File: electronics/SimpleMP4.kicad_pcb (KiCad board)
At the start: 2 copper layers, 136.9 x 66.4 mm, 130 parts, among them J1 USB_OTG, J2 DISPLAY, Q1 8050, Q2 SI2305, Q3 SI2305, Q4 8050, Q5 8550, Q6 SI2305, Q7 8550, U1 OCP8020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

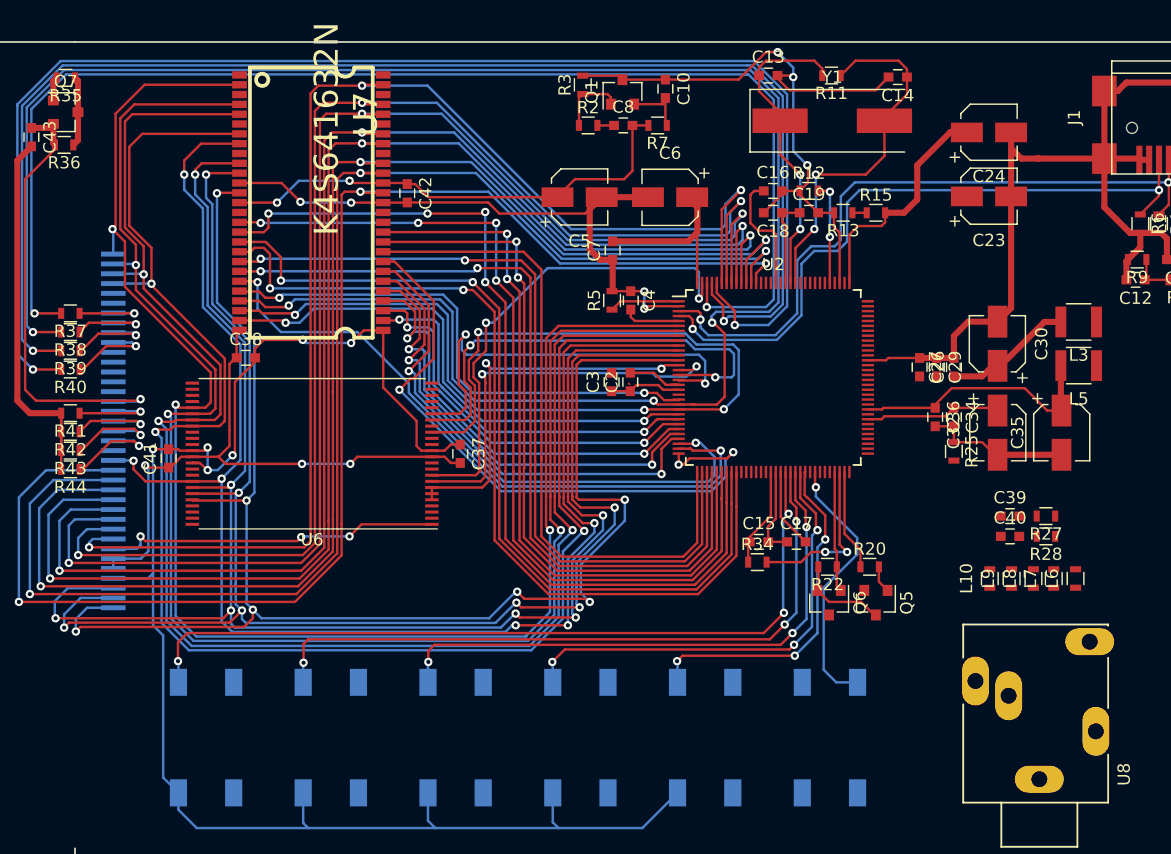
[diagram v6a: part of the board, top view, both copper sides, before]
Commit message: routed headphone jack
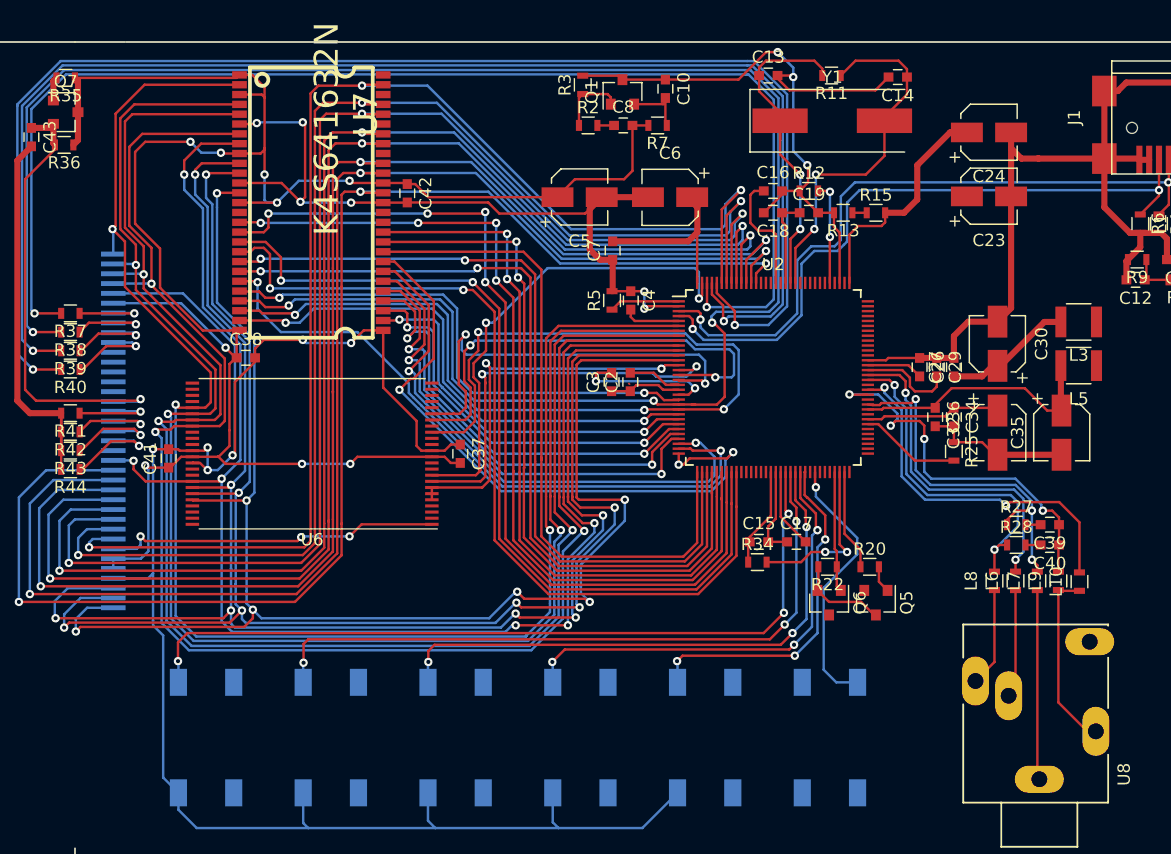
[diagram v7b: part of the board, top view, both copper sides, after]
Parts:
- moved L10 7.31 mm to (150.7, 170.3)
- moved L6 4.89 mm to (145.5, 170.2)
- moved L9 3.81 mm to (149.0, 170.2)
- moved C39 3.31 mm to (148.3, 165.7), turned to 180 degrees
- moved C40 3.31 mm to (148.3, 167.3), turned to 180 degrees
- moved L8 3.18 mm to (143.8, 170.2)
- moved R27 2.51 mm to (145.6, 165.7), turned to 0 degrees
- moved R28 2.51 mm to (145.6, 167.3), turned to 0 degrees
- moved L7 1.35 mm to (147.3, 170.2)
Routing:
- net VCC: track 174.1 -> 257.4 mm, vias 5 -> 11
- net GND: track 486.2 -> 518.8 mm, vias 18 -> 20
- net /AOM: track 0.00 -> 31.2 mm, vias 0 -> 4
- net /AOMS: track 0.00 -> 29.6 mm, vias 0 -> 2
- net /AOL: track 0.00 -> 29.0 mm, vias 0 -> 3
- net /AOR: track 0.00 -> 27.7 mm, vias 0 -> 2
- net /HP_SENSE: track 0.00 -> 27.1 mm, vias 0 -> 2
- net Net-(L7-Pad1): track 0.00 -> 15.5 mm
- net Net-(L10-Pad1): track 0.00 -> 14.9 mm
- net Net-(L6-Pad1): track 0.00 -> 8.84 mm
- net Net-(R25-Pad2): track 0.00 -> 8.24 mm
- net Net-(L8-Pad1): track 0.00 -> 8.05 mm
- net Net-(C29-Pad2): track 0.00 -> 7.73 mm
- net Net-(C26-Pad2): track 0.00 -> 4.59 mm
- net Net-(C40-Pad2): track 0.00 -> 1.23 mm
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
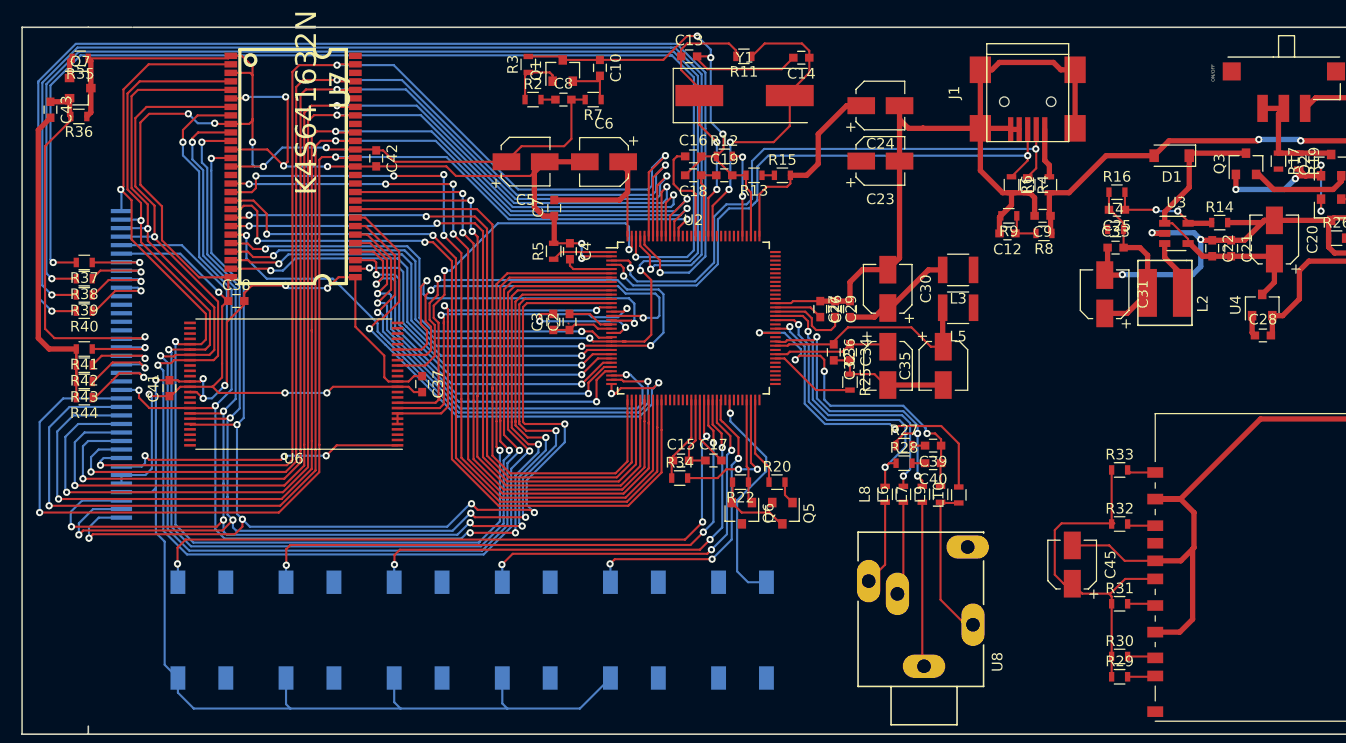
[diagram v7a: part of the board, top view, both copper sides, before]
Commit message: routed most connections
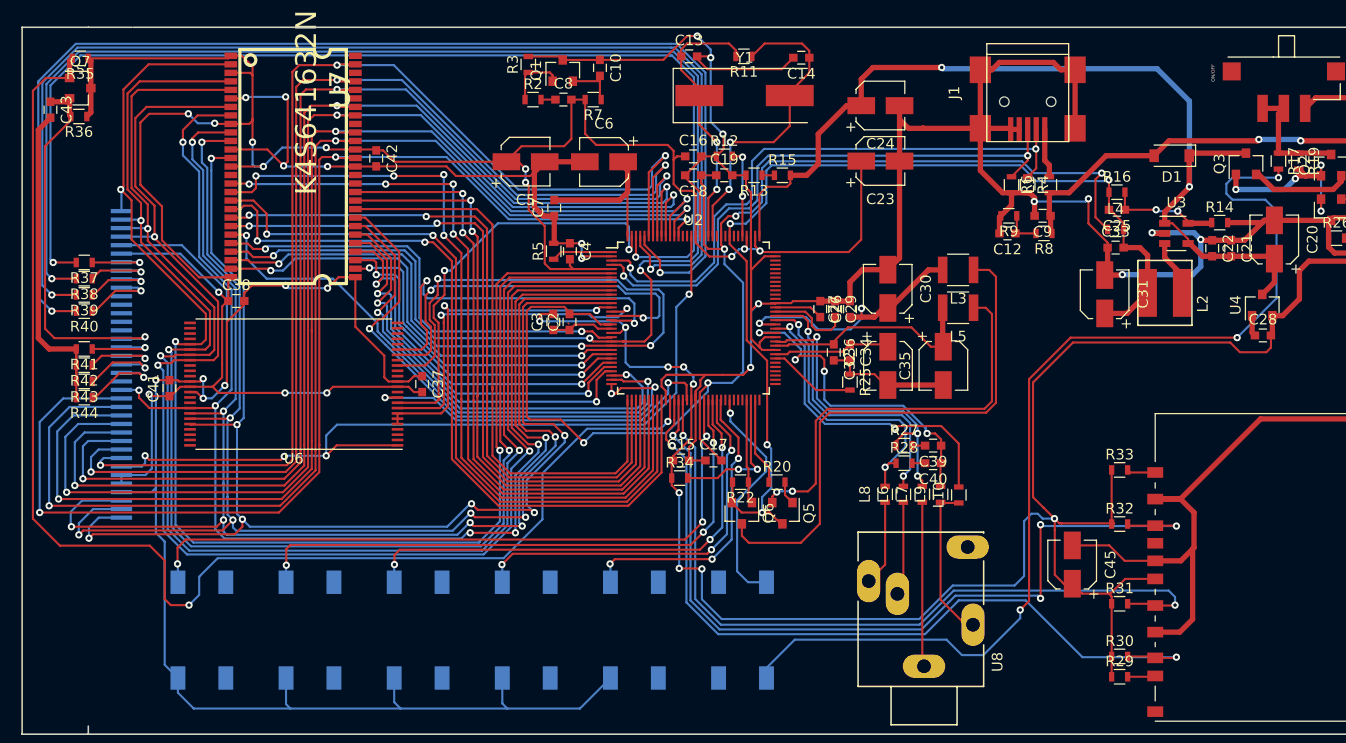
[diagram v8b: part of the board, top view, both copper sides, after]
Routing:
- net VCC: track 257.4 -> 420.8 mm, vias 11 -> 23
- net /LIGHT_CON: track 1.95 -> 124.1 mm, vias 0 -> 2
- net /VDD: track 18.8 -> 124.1 mm, vias 0 -> 5
- net Net-(B1-Pad1): track 0.00 -> 97.6 mm, vias 0 -> 3
- net /SDDI: track 2.66 -> 79.6 mm, vias 0 -> 4
- net /SDDO: track 2.65 -> 75.8 mm, vias 0 -> 2
- net /VDDO: track 24.3 -> 94.9 mm, vias 0 -> 4
- net /SDCLK: track 2.66 -> 72.2 mm, vias 0 -> 2
- net GND: track 518.8 -> 578.7 mm, vias 20 -> 24
- net /RESETN: track 32.7 -> 84.5 mm, vias 3 -> 4
- net /VDDAO: track 0.00 -> 50.5 mm
- net /BATT: track 47.5 -> 90.8 mm, vias 0 -> 2
- net /VDDA: track 0.00 -> 38.6 mm, vias 0 -> 2
- net /FCE1: track 0.00 -> 34.0 mm, vias 0 -> 2
- net Net-(C27-Pad1): track 10.5 -> 24.7 mm, vias 0 -> 2
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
